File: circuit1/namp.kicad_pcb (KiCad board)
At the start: 2 copper layers, 159 x 111.5 mm, 97 parts, among them J1 Screw_Terminal_01x08, J2 Screw_Terminal_01x04, J3 Screw_Terminal_01x04, J4 Conn_01x08_Female, U1 NRF52840-DONGLE, U2 MCP6004, U3 MCP6004, U4 MCP1501-33xSN, U5 MCP3564, U6 MCP1754S-5002xCB, U7 MCP1754S-5002xCB, U8 MCP1754S-3302xCB

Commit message: update
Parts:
- added J5: Conn_01x08_Male, Connector_PinHeader_2.54mm:PinHeader_1x08_P2.54mm_Vertical, F.Cu at (181.1, 128.5)
- moved J3 78.3 mm to (101.6, 99.1), turned to -90 degrees
- moved C37 67.7 mm to (157.9, 126.5), turned to -90 degrees
- moved C39 64.7 mm to (160.5, 129.4), turned to 180 degrees
- moved U8 63.9 mm to (160.5, 126.6), turned to 90 degrees
- moved J2 26.3 mm to (101.9, 116.3), turned to -90 degrees
- moved R26 18.2 mm to (140.2, 90.0)
- moved R30 18.2 mm to (132.5, 112.9)
- moved R41 18.2 mm to (149.6, 112.1)
- moved C28 18.2 mm to (153.4, 112.1)
- moved R25 18.2 mm to (142.7, 90.0)
- moved R27 18.2 mm to (142.7, 112.9)
- moved R28 18.2 mm to (145.2, 112.9)
- moved R29 18.2 mm to (137.6, 90.0)
- moved R31 18.2 mm to (136.1, 105.5)
- moved R32 18.2 mm to (137.6, 112.9)
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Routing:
- net PWR_MAX16V: track 11.6 -> 170.6 mm, vias 0 -> 4
- net ADC_CS: track 0.00 -> 26.8 mm
- net ADC_SCK: track 0.00 -> 24.4 mm
- net ADC_SDI: track 0.00 -> 20.8 mm
- net ADC_SDO: track 0.00 -> 18.6 mm
- net ADC_INT: track 0.00 -> 18.2 mm
- net ADC_MCK: track 0.00 -> 12.4 mm
- net ADC_DVDD: track 4.28 -> 14.2 mm
- net GND: track 71.1 -> 78.7 mm, vias 21 -> 23
- net Net-(C39-Pad1): track 0.00 -> 4.11 mm
- net ADC_AVDD: track 4.49 -> 5.90 mm
- net /ADC_CH7: track 66.7 -> 68.0 mm
- net /ADC_CH6: track 40.9 -> 41.7 mm
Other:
- board size 159 x 111.5 mm -> 88.9 x 71.1 mm
- board text added: "CH0"
- board text added: "CH1"
- board text added: "CH2"
- board text added: "CH3"
- board text added: "CH4"
- board text added: "CH5"
- board text added: "CH6"
- board text added: "CH7"
- board text added: "CS"
- board text added: "DVDD"
- board text added: "GND"
- board text added: "INT"
- board text added: "MCK"
- board text added: "PWR"
- board text added: "SCK"
- board text added: "SDI"
- board text added: "SDO"

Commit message: update
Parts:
- removed R26, R27, R29: 100, Resistor_SMD:R_0603_1608Metric
- moved R41 27.7 mm to (170.2, 130.6), turned to 90 degrees
- moved R25 23.0 mm to (142.7, 113.0), turned to -90 degrees
- moved R31 7.59 mm to (135.1, 113.0), turned to -90 degrees
- moved U7 1.32 mm to (152.7, 115.1)
- moved C36 1.07 mm to (155.4, 115.2)
- moved C35 1.06 mm to (152.4, 117.7)
- moved C28 0.27 mm to (153.7, 112.1)
- moved C38 0.18 mm to (159.6, 133.9)
- moved R28 0.16 mm to (145.2, 113.0), turned to -90 degrees
- moved R30 0.16 mm to (132.5, 113.0)
- moved R32 0.16 mm to (137.6, 113.0)
- moved C31 0.13 mm to (161.3, 133.9)
- moved R42 0.13 mm to (171.7, 130.6)
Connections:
- R25 pad 1: Net-(R25-Pad1) -> Net-(U1-Pad0.29)
- R25 pad 2: unconnected-(R25-Pad2) -> ADC_SDO
- R30 pad 2: ADC_SDI -> ADC_CS
- R32 pad 2: ADC_CS -> ADC_SDI
- U1 pad 0.22: Net-(R25-Pad1) -> unconnected-(U1-Pad0.22)
- U1 pad 0.24: Net-(R26-Pad1) -> unconnected-(U1-Pad0.24)
- U1 pad 0.29: Net-(R27-Pad1) -> Net-(U1-Pad0.29)
- U1 pad 1.00: Net-(R29-Pad1) -> unconnected-(U1-Pad1.00)
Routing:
- net NRF_REG0_V: track 0.00 -> 46.7 mm
- net ADC_CS: track 26.8 -> 67.9 mm, vias 0 -> 2
- net ADC_SCK: track 24.4 -> 64.7 mm, vias 0 -> 2
- net ADC_SDI: track 20.8 -> 60.2 mm, vias 0 -> 2
- net ADC_SDO: track 18.6 -> 54.7 mm, vias 0 -> 2
- net ADC_INT: track 18.2 -> 53.5 mm, vias 0 -> 2
- net NRF_VBUS: track 0.00 -> 7.17 mm
- net GND: track 78.7 -> 85.0 mm, vias 23 -> 25
- net Net-(C11-Pad2): track 3.75 -> 6.87 mm
- net Net-(U1-Pad0.29): track 0.00 -> 3.00 mm
- net Net-(R31-Pad1): track 0.00 -> 3.00 mm
- net Net-(U1-Pad1.10): track 0.00 -> 2.99 mm
- net Net-(R32-Pad1): track 0.00 -> 2.99 mm
- net Net-(R28-Pad1): track 0.00 -> 2.99 mm
- net PWR_MAX16V: track 170.6 -> 173.5 mm
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
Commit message: update
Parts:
- U5: value MCP3564 -> TSSOP20_ST_MCH

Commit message: update
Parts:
- added R26: 10, Resistor_SMD:R_0603_1608Metric, F.Cu at (160.8, 153.4)
- U5: value TSSOP20_ST_MCH -> MCP3564
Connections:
- net TIA_V renamed TIA_5V
- C26 pad 1: PWR_MAX16V -> Net-(C26-Pad1)
- U4 pad 1: PWR_MAX16V -> Net-(C26-Pad1)
- U4 pad 3: PWR_MAX16V -> Net-(C26-Pad1)
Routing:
- net PWR_MAX16V: track 173.5 -> 92.9 mm, vias 4 -> 0
- net TIA_5V: track 30.6 -> 89.6 mm
- net Net-(C26-Pad1): track 0.00 -> 11.1 mm
- net ADC_SCK: track 64.7 -> 64.2 mm
- net ADC_CS: track 67.9 -> 67.4 mm
- net /CH0: vias 0 -> 1
- net /CH7: vias 0 -> 1

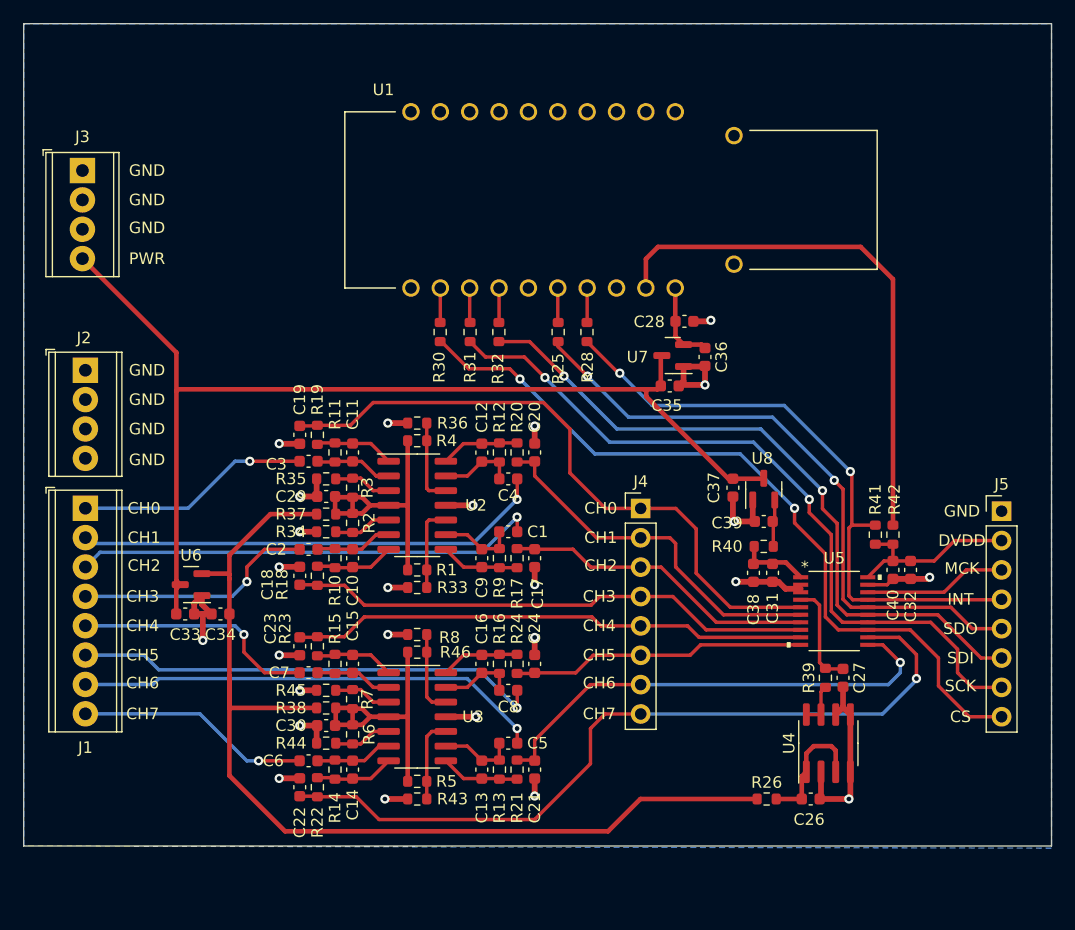
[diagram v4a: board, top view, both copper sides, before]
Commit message: Changed to 0805
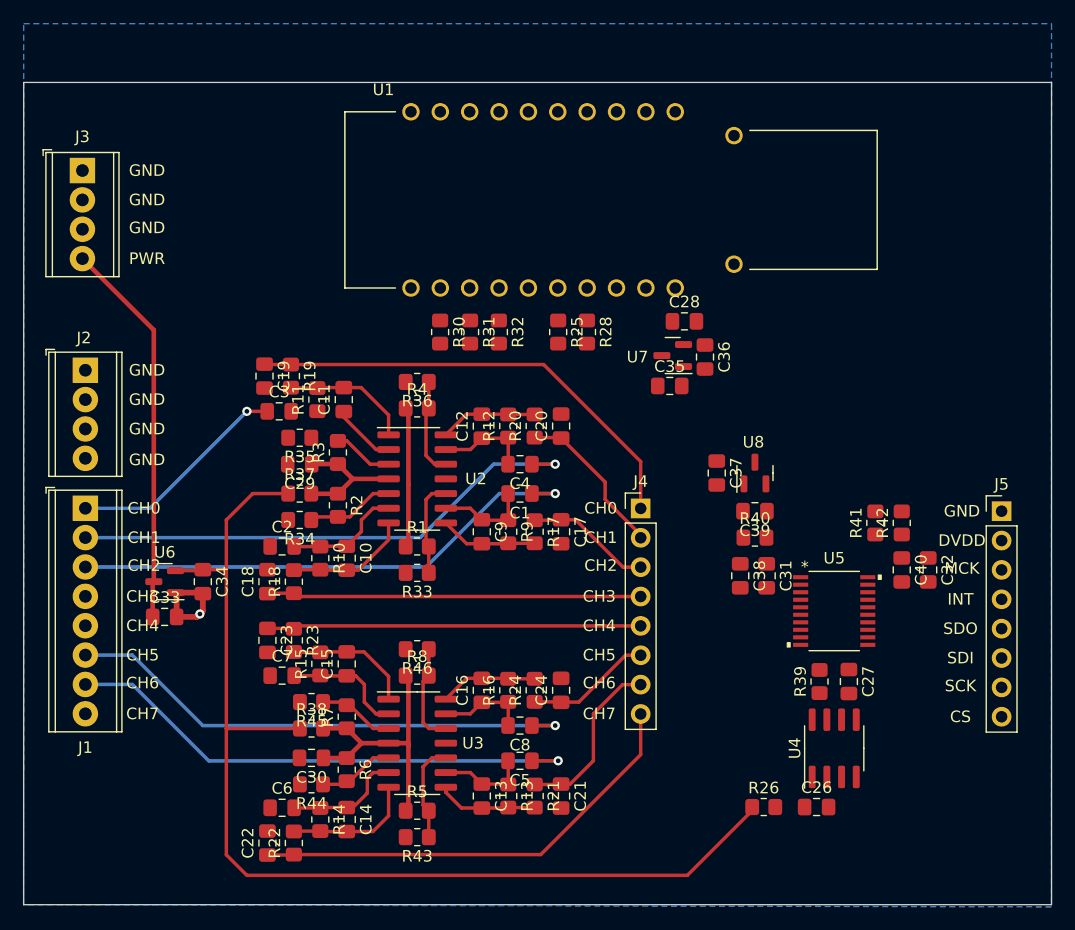
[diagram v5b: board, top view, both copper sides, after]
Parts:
- C1, C10, C11, C12, C13, C14, C15, C16, C17, C18, C19, C2, C20, C21, C22, C23, C24, C26, C27, C28, C29, C3, C30, C31, C32, C33, C34, C35, C36, C37, C38, C39, C4, C40, C5, C6, C7, C8, C9: footprint Capacitor_SMD:C_0603_1608Metric -> Capacitor_SMD:C_0805_2012Metric_Pad1.18x1.45mm_HandSolder
- R1, R10, R11, R12, R13, R14, R15, R16, R17, R18, R19, R2, R20, R21, R22, R23, R24, R25, R26, R28, R3, R30, R31, R32, R33, R34, R35, R36, R37, R38, R39, R4, R40, R41, R42, R43, R44, R45, R46, R5, R6, R7, R8, R9: footprint Resistor_SMD:R_0603_1608Metric -> Resistor_SMD:R_0805_2012Metric_Pad1.20x1.40mm_HandSolder
- moved C19 5.92 mm to (117.3, 116.8)
- moved C22 5.58 mm to (117.6, 157.2)
- moved R19 5.57 mm to (119.6, 116.8)
- moved R22 5.24 mm to (119.9, 157.2)
- moved C3 5.01 mm to (118.6, 119.9)
- moved R11 4.82 mm to (121.9, 118.9)
- moved C6 4.66 mm to (118.9, 154.2)
- moved C11 4.64 mm to (124.2, 118.9)
- moved R14 4.50 mm to (122.2, 155.2)
- moved C14 4.35 mm to (124.5, 155.2)
- moved R35 4.23 mm to (120.4, 122.2)
- moved R44 3.78 mm to (121.4, 152.1)
- moved C29 3.61 mm to (120.4, 124.5)
- moved R36 3.56 mm to (130.6, 117.3)
- moved C1 3.45 mm to (139.4, 127.0)
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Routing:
- net GND: track 85.0 -> 8.52 mm, vias 25 -> 1
- net ADC_CS: track 67.4 -> 0.00 mm, vias 2 -> 0
- net ADC_SCK: track 64.2 -> 0.00 mm, vias 2 -> 0
- net ADC_SDI: track 59.9 -> 0.00 mm, vias 2 -> 0
- net PWR_MAX16V: track 92.9 -> 33.6 mm
- net ADC_SDO: track 54.6 -> 0.00 mm, vias 2 -> 0
- net ADC_INT: track 53.7 -> 0.00 mm, vias 2 -> 0
- net NRF_REG0_V: track 46.7 -> 0.00 mm
- net /ADC_CH7: track 68.0 -> 39.4 mm, vias 1 -> 0
- net /ADC_CH6: track 41.7 -> 15.1 mm, vias 1 -> 0
- net /CH4: track 21.1 -> 0.00 mm, vias 1 -> 0
- net /CH3: track 21.0 -> 0.00 mm, vias 1 -> 0
- net /CH7: track 20.2 -> 0.00 mm, vias 1 -> 0
- net /ADC_CH1: track 32.0 -> 13.8 mm
- net /ADC_CH2: track 27.2 -> 10.9 mm
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
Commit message: update
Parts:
- moved C35 17.1 mm to (149.4, 100.8), turned to -90 degrees
- moved U7 14.0 mm to (152.0, 101.1), turned to 90 degrees
- moved C36 11.9 mm to (151.9, 103.9), turned to 180 degrees
- moved C28 10.1 mm to (155.0, 102.1), turned to -90 degrees
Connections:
- U5 pad 11: /ADC_CH6 -> /ADC_CH7
- U5 pad 12: /ADC_CH7 -> /ADC_CH6
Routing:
- net GND: track 8.52 -> 70.7 mm, vias 1 -> 22
- net PWR_MAX16V: track 33.6 -> 87.0 mm
- net /ADC_CH7: track 39.4 -> 67.1 mm, vias 0 -> 1
- net /ADC_CH6: track 15.1 -> 40.3 mm, vias 0 -> 1
- net /ADC_CH0: track 40.1 -> 61.2 mm
- net /CH7: track 0.00 -> 19.3 mm, vias 0 -> 1
- net /CH4: track 0.00 -> 17.8 mm, vias 0 -> 1
- net /CH3: track 0.00 -> 17.8 mm, vias 0 -> 1
- net /ADC_CH1: track 13.8 -> 31.4 mm
- net /ADC_CH2: track 10.9 -> 26.7 mm
- net /ADC_CH3: track 32.4 -> 47.4 mm
- net /ADC_CH4: track 32.4 -> 46.7 mm
- net /ADC_CH5: track 10.9 -> 25.1 mm
- net Net-(C26-Pad1): track 0.00 -> 12.4 mm
- net ADC_VREF+: track 0.00 -> 9.98 mm
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
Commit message: update
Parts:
- moved C35 24.0 mm to (170.7, 111.8), turned to 90 degrees
- moved U7 18.7 mm to (167.1, 112.0), turned to -90 degrees
- moved C36 16.0 mm to (167.1, 108.7), turned to 0 degrees
- moved C28 12.6 mm to (163.1, 111.8)
- moved C33 3.31 mm to (109.0, 134.4), turned to -90 degrees
- moved U6 3.31 mm to (112.0, 134.4), turned to 90 degrees
- moved C34 3.05 mm to (112.0, 137.7), turned to 180 degrees
- moved R25 2.29 mm to (142.7, 110.7)
- moved R28 2.29 mm to (145.2, 110.7)
- moved R30 2.29 mm to (132.5, 110.7)
- moved R31 2.29 mm to (135.1, 110.7)
- moved R32 2.29 mm to (137.6, 110.7)
- moved U1 2.29 mm to (147.3, 99.3)
- moved C32 0.76 mm to (174.8, 132.8)
- moved C40 0.76 mm to (172.5, 132.8)
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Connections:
- U5 pad 11: /ADC_CH7 -> /ADC_CH6
- U5 pad 12: /ADC_CH6 -> /ADC_CH7
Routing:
- net PWR_MAX16V: track 87.0 -> 186.7 mm, vias 0 -> 1
- net ADC_CS: track 0.00 -> 73.9 mm
- net ADC_SCK: track 0.00 -> 69.1 mm
- net ADC_SDI: track 0.00 -> 64.5 mm
- net ADC_SDO: track 0.00 -> 57.3 mm
- net ADC_INT: track 0.00 -> 56.0 mm
- net GND: track 70.7 -> 103.9 mm, vias 22 -> 29
- net NRF_REG0_V: track 0.00 -> 32.8 mm
- net ADC_DVDD: track 0.00 -> 17.2 mm
- net ADC_MCK: track 0.00 -> 12.4 mm
- net ADC_AVDD: track 0.00 -> 8.14 mm
- net NRF_VBUS: track 9.63 -> 17.4 mm
- net TIA_5V: track 94.9 -> 101.8 mm
- net /ADC_CH7: track 67.1 -> 72.0 mm
- net Net-(C39-Pad1): track 0.00 -> 4.70 mm
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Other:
- board size 88.9 x 71.1 mm -> 88.9 x 76.2 mm

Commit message: added holes
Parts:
- added REF**: MountingHole_3.2mm_M3, MountingHole:MountingHole_3.2mm_M3, F.Cu at (181.5, 157.6)
- added REF**: MountingHole_3.2mm_M3, MountingHole:MountingHole_3.2mm_M3, F.Cu at (101.5, 157.6)
- added REF**: MountingHole_3.2mm_M3, MountingHole:MountingHole_3.2mm_M3, F.Cu at (181.5, 92.6)
- added REF**: MountingHole_3.2mm_M3, MountingHole:MountingHole_3.2mm_M3, F.Cu at (101.5, 92.6)
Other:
- board size 88.9 x 76.2 mm -> 90 x 75 mm
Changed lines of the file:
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@@
     )
     (pad_to_mask_clearance 0)
+    (grid_origin 96.52 162.56)
     (pcbplotparams
       (layerselection 0x00010fc_ffffffff)
@@
     )
   )
+  (footprint "MountingHole:MountingHole_3.2mm_M3" (layer "F.Cu")
+    (at 181.52 157.56)
+    (descr "Mounting Hole 3.2mm, no annular, M3")
+    (tags "mounting hole 3.2mm no annular m3")
+    (attr exclude_from_pos_files exclude_from_bom)
+    (fp_text reference "REF**" (at 0 -4.2) (layer "F.SilkS")
+      (effects (font (size 1 1) (thickness 0.15)))
+    )
+    (fp_text value "MountingHole_3.2mm_M3" (at 0 4.2) (layer "F.Fab")
+      (effects (font (size 1 1) (thickness 0.15)))
+    )
+    (fp_text user "${REFERENCE}" (at 0.3 0) (layer "F.Fab")
+      (effects (font (size 1 1) (thickness 0.15)))
+    )
+    (fp_circle (center 0 0) (end 3.2 0) (layer "Cmts.User") (width 0.15) (fill none))
+    (fp_circle (center 0 0) (end 3.45 0) (layer "F.CrtYd") (width 0.05) (fill none))
+    (pad "" np_thru_hole circle (at 0 0) (size 3.2 3.2) (drill 3.2) (layers *.Cu *.Mask))
+  )
   (footprint "Resistor_SMD:R_0805_2012Metric_Pad1.20x1.40mm_HandSolder" (layer "F.Cu")
     (at 170.18 128.778 90)
@@
     )
   )
+  (footprint "MountingHole:MountingHole_3.2mm_M3" (layer "F.Cu")
+    (at 101.52 157.56)
+    (descr "Mounting Hole 3.2mm, no annular, M3")
+    (tags "mounting hole 3.2mm no annular m3")
+    (attr exclude_from_pos_files exclude_from_bom)
+    (fp_text reference "REF**" (at 0 -4.2) (layer "F.SilkS")
+      (effects (font (size 1 1) (thickness 0.15)))
+    )
+    (fp_text value "MountingHole_3.2mm_M3" (at 0 4.2) (layer "F.Fab")
+      (effects (font (size 1 1) (thickness 0.15)))
+    )
+    (fp_text user "${REFERENCE}" (at 0.3 0) (layer "F.Fab")
+      (effects (font (size 1 1) (thickness 0.15)))
+    )
+    (fp_circle (center 0 0) (end 3.2 0) (layer "Cmts.User") (width 0.15) (fill none))
+    (fp_circle (center 0 0) (end 3.45 0) (layer "F.CrtYd") (width 0.05) (fill none))
+    (pad "" np_thru_hole circle (at 0 0) (size 3.2 3.2) (drill 3.2) (layers *.Cu *.Mask))
+  )
   (footprint "Resistor_SMD:R_0805_2012Metric_Pad1.20x1.40mm_HandSolder" (layer "F.Cu")
     (at 140.716 153.162 -90)
@@
     )
   )
+  (footprint "MountingHole:MountingHole_3.2mm_M3" (layer "F.Cu")
+    (at 181.52 92.56)
+    (descr "Mounting Hole 3.2mm, no annular, M3")
+    (tags "mounting hole 3.2mm no annular m3")
+    (attr exclude_from_pos_files exclude_from_bom)
+    (fp_text reference "REF**" (at 0 -4.2) (layer "F.SilkS")
+      (effects (font (size 1 1) (thickness 0.15)))
+    )
+    (fp_text value "MountingHole_3.2mm_M3" (at 0 4.2) (layer "F.Fab")
+      (effects (font (size 1 1) (thickness 0.15)))
+    )
+    (fp_text user "${REFERENCE}" (at 0.3 0) (layer "F.Fab")
+      (effects (font (size 1 1) (thickness 0.15)))
+    )
+    (fp_circle (center 0 0) (end 3.2 0) (layer "Cmts.User") (width 0.15) (fill none))
+    (fp_circle (center 0 0) (end 3.45 0) (layer "F.CrtYd") (width 0.05) (fill none))
+    (pad "" np_thru_hole circle (at 0 0) (size 3.2 3.2) (drill 3.2) (layers *.Cu *.Mask))
+  )
   (footprint "Capacitor_SMD:C_0805_2012Metric_Pad1.18x1.45mm_HandSolder" (layer "F.Cu")
     (at 143.002 153.162 -90)
@@
     )
   )
+  (footprint "MountingHole:MountingHole_3.2mm_M3" (layer "F.Cu")
+    (at 101.52 92.56)
+    (descr "Mounting Hole 3.2mm, no annular, M3")
+    (tags "mounting hole 3.2mm no annular m3")
+    (attr exclude_from_pos_files exclude_from_bom)
+    (fp_text reference "REF**" (at 0 -4.2) (layer "F.SilkS")
+      (effects (font (size 1 1) (thickness 0.15)))
+    )
+    (fp_text value "MountingHole_3.2mm_M3" (at 0 4.2) (layer "F.Fab")
+      (effects (font (size 1 1) (thickness 0.15)))
+    )
+    (fp_text user "${REFERENCE}" (at 0.3 0) (layer "F.Fab")
+      (effects (font (size 1 1) (thickness 0.15)))
+    )
+    (fp_circle (center 0 0) (end 3.2 0) (layer "Cmts.User") (width 0.15) (fill none))
+    (fp_circle (center 0 0) (end 3.45 0) (layer "F.CrtYd") (width 0.05) (fill none))
+    (pad "" np_thru_hole circle (at 0 0) (size 3.2 3.2) (drill 3.2) (layers *.Cu *.Mask))
+  )
   (footprint "Resistor_SMD:R_0805_2012Metric_Pad1.20x1.40mm_HandSolder" (layer "F.Cu")
     (at 140.716 130.302 -90)
@@
     )
   )
-  (gr_rect (start 96.52 86.36) (end 185.42 162.56) (layer "Edge.Cuts") (width 0.1) (fill none))
+  (gr_rect (start 96.52 87.56) (end 186.52 162.56) (layer "Edge.Cuts") (width 0.1) (fill none))
+  (gr_line (start 181.52 92.56) (end 101.52 92.56) (layer "User.1") (width 0.15))
+  (gr_line (start 101.52 157.56) (end 181.52 157.56) (layer "User.1") (width 0.15))
+  (gr_line (start 181.52 157.56) (end 181.52 92.56) (layer "User.1") (width 0.15))
   (gr_line (start 177.292 137.16) (end 93.98 137.16) (layer "User.1") (width 0.15))
+  (gr_line (start 101.52 92.56) (end 101.52 157.56) (layer "User.1") (width 0.15))
   (gr_text "GND" (at 107.188 104.013) (layer "F.SilkS")
     (effects (font (size 1 1) (thickness 0.15)))
@@
     (polygon
       (pts
-        (xy 185.409095 162.750807)
+        (xy 186.52 162.750807)
         (xy 96.509095 162.559976)
-        (xy 96.52 86.36)
-        (xy 185.42 86.36)
+        (xy 96.52 87.56)
+        (xy 186.52 87.56)
       )
     )
